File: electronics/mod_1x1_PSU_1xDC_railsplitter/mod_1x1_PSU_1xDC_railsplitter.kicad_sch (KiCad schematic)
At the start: 11 parts, among them J1 module_2x15_left_input, J2 module_2x15_right_input, J3 Jack-DC, J5 Conn_01x02

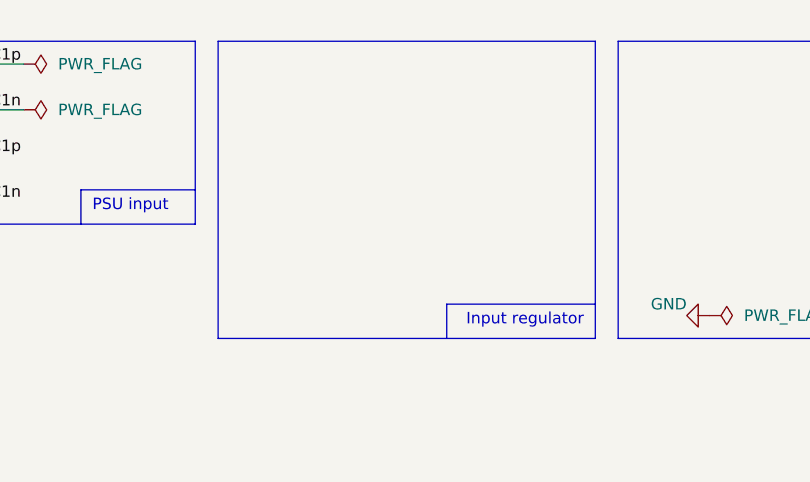
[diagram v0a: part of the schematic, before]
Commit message: WIP initial LDO schematic, updated PCB library
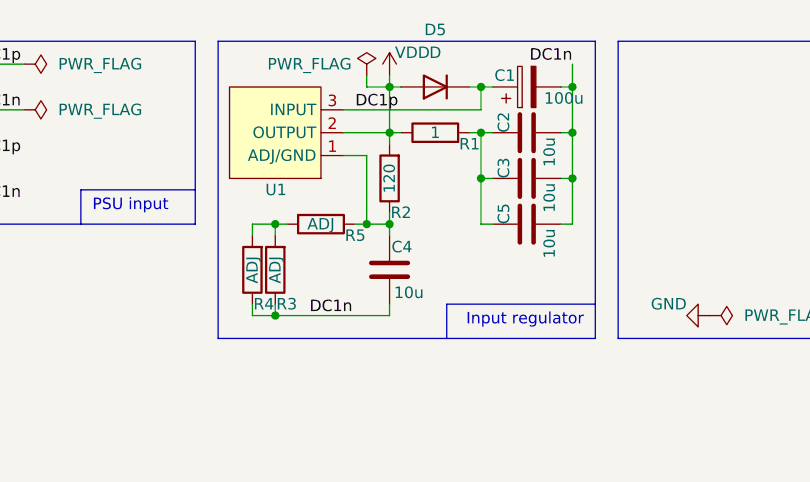
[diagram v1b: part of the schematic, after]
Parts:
- added C1: 100u, SquantorRcl:C-050-100-elco, symbol Device:C_Polarized
- added C2, C3, C4, C5: 10u, SquantorRcl:C_0805, symbol Device:C
- added D5: D, SquantorDiodes:SOD-323-onsemi, symbol Device:D
- added R1: 1, SquantorRcl:R_0805+0603, symbol Device:R
- added R2: 120, SquantorRcl:R_0805+0603, symbol Device:R
- added R3, R4, R5: ADJ, SquantorRcl:R_0805+0603, symbol Device:R
- added U1: ~, SquantorIC:TO-252_D-PAK_IRF, symbol SquantorGenericAnalog:LM1117
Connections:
- net DC1n: now also C1.2, C2.2, C3.2, C4.1, C5.2, R3.1, R4.1
- net DC1p: now also C1.1, D5.1 (K), U1.3 (INPUT)
- new net: C2.1, C3.1, C5.1, R1.2
- new net: C4.2, R2.1, R5.1, U1.1 (ADJ/GND)
- new net: R3.2, R4.2, R5.2
- new net VDD: D5.2 (A), R1.1, R2.2, U1.2 (OUTPUT)

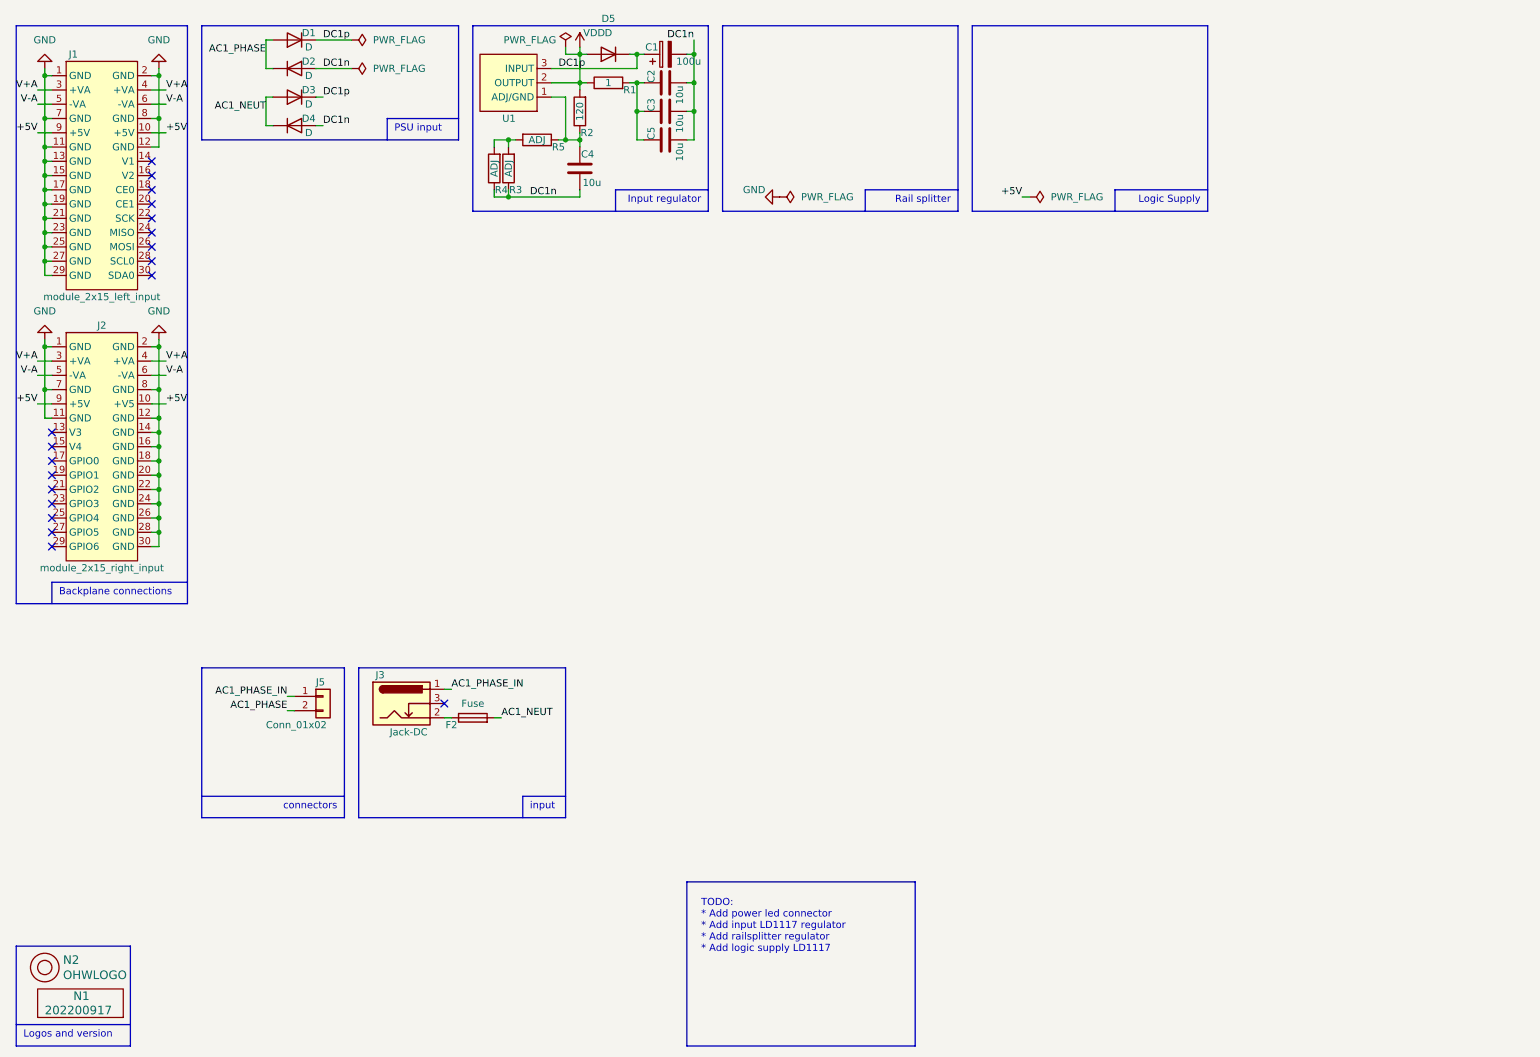
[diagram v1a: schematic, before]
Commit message: WIP schematic entry
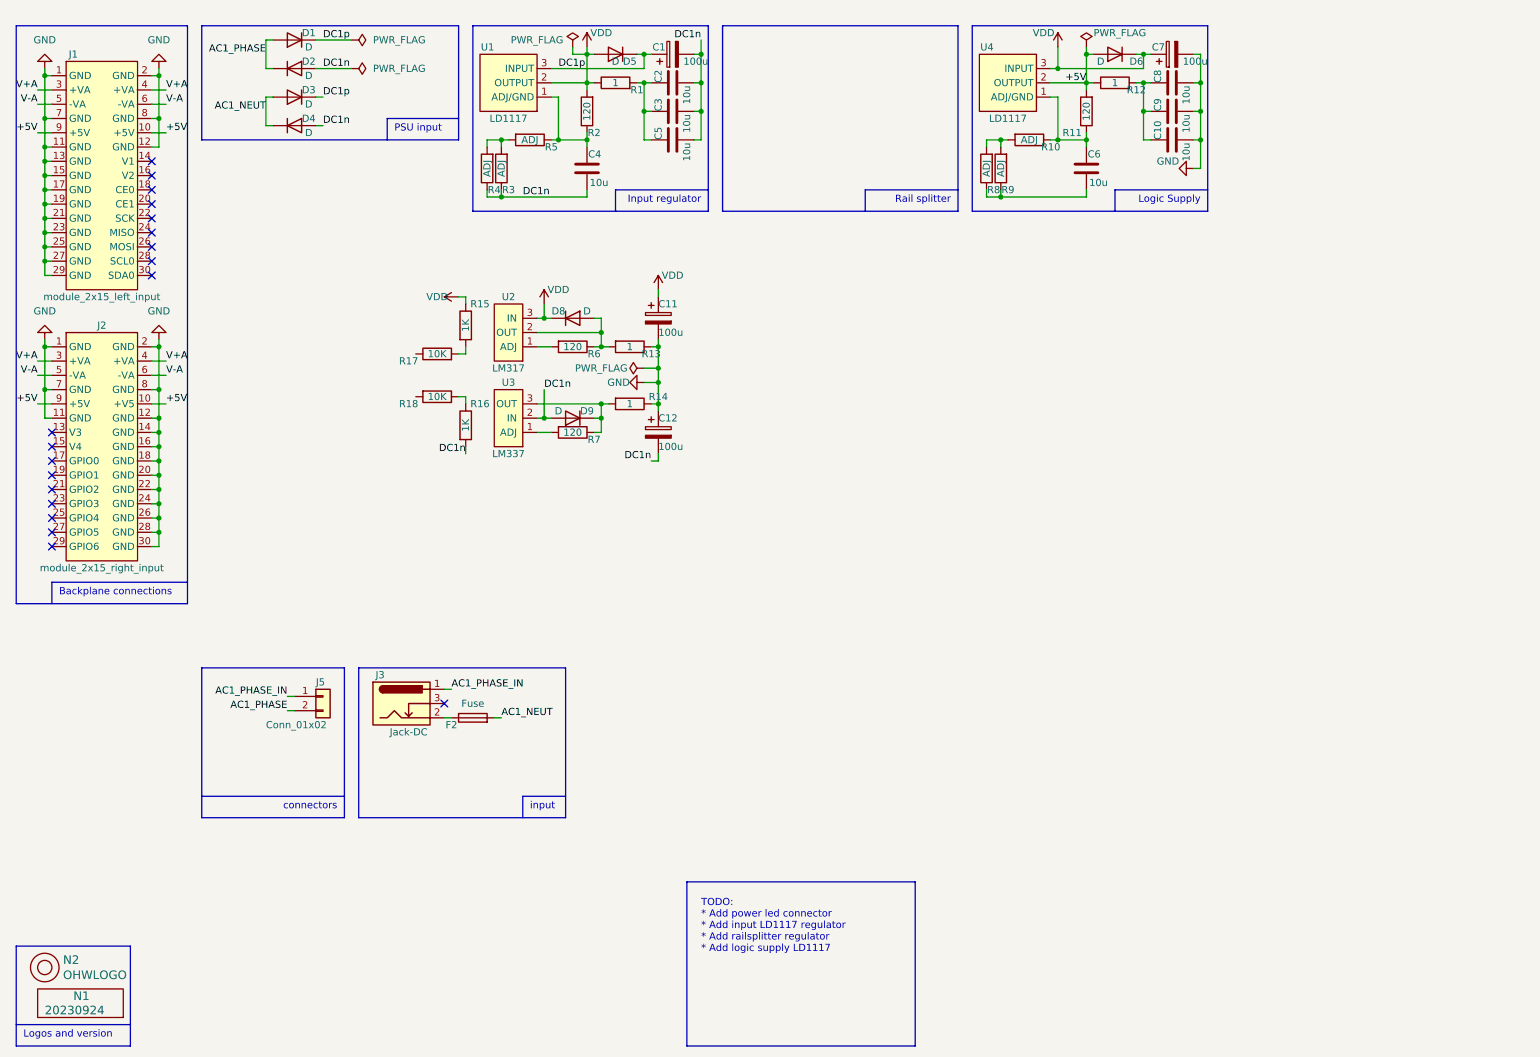
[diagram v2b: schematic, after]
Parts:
- added C10, C6, C8, C9: 10u, SquantorRcl:C_0805, symbol Device:C
- added C11, C12, C7: 100u, SquantorRcl:C-050-100-elco-lying, symbol Device:C_Polarized
- added D6, D8, D9: D, SquantorDiodes:SOD-323-onsemi, symbol Device:D
- added R10, R8, R9: ADJ, SquantorRcl:R_0805+0603, symbol Device:R
- added R11, R6, R7: 120, SquantorRcl:R_0805+0603, symbol Device:R
- added R12, R13, R14: 1, SquantorRcl:R_0805+0603, symbol Device:R
- added R15, R16: 1K, SquantorRcl:R_0805+0603, symbol Device:R
- added R17, R18: 10K, SquantorRcl:R_0805+0603, symbol Device:R
- added U2: LM317, SquantorIC:TO-252_D-PAK_IRF, symbol SquantorGenericAnalog:LM317
- added U3: LM337, SquantorIC:TO-252_D-PAK_IRF, symbol SquantorGenericAnalog:LM337
- added U4: LD1117, SquantorIC:TO-252_D-PAK_IRF, symbol SquantorGenericAnalog:LM1117
- C1: footprint SquantorRcl:C-050-100-elco -> SquantorRcl:C-050-100-elco-lying
- N1: value 202200917 -> 20230924
- U1: value ~ -> LD1117
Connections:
- net +5V: now also D6.2 (A), R11.2, R12.1, U4.2 (OUTPUT)
- net DC1n: now also C12.2, D9.2 (A), R16.2, U3.2 (IN)
- net GND: now also C10.2, C11.2, C12.1, C7.2, C8.2, C9.2, R13.1, R14.1
- net VDD: now also C11.1, C7.1, D6.1 (K), D8.1 (K), R15.1, U2.3 (IN), U4.3 (INPUT)
- new net: R7.2, U3.1 (ADJ)
- new net: D9.1 (K), R14.2, R7.1, U3.3 (OUT)
- new net: D8.2 (A), R13.2, R6.1, U2.2 (OUT)
- new net: R15.2, R17.2
- new net: C6.2, R10.1, R11.1, U4.1 (ADJ/GND)
- new net: R10.2, R8.2, R9.2
- new net: C6.1, R8.1, R9.1
- new net: C10.1, C8.1, C9.1, R12.2
- new net: R16.1, R18.1
- new net: R6.2, U2.1 (ADJ)
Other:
- moved on the sheet: C1, C2, C3, C4, C5, D5, R1, R2, R3, R4, R5

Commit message: small schematic updates and place and route
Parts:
- added RV1: 1K, Potentiometer_THT:Potentiometer_Bourns_3386P_Vertical, symbol Device:R_Potentiometer
- C1: footprint SquantorRcl:C-050-100-elco-lying -> SquantorRcl:C-050-100-elco-lying_flip
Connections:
- net GND: now also C6.1, R8.1, R9.1
- net at R17.1: now also R15.2
- net at R17.2: now also RV1.1; no longer R15.2
- net at R18.2: now also RV1.3
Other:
- moved on the sheet: R15, R16, R17, R18

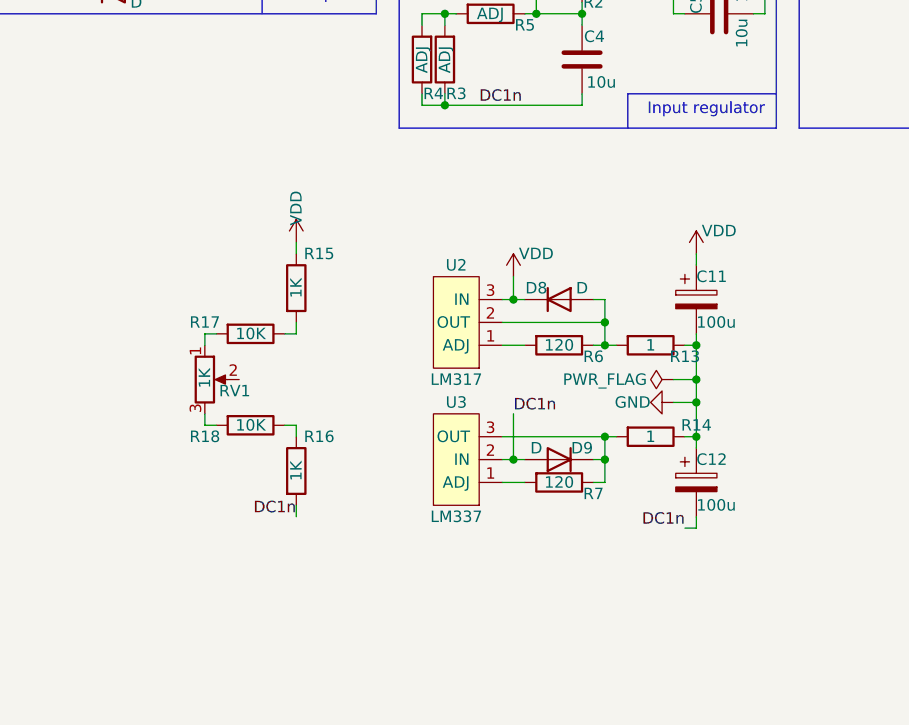
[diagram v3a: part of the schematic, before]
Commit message: WIP placement, done schematic
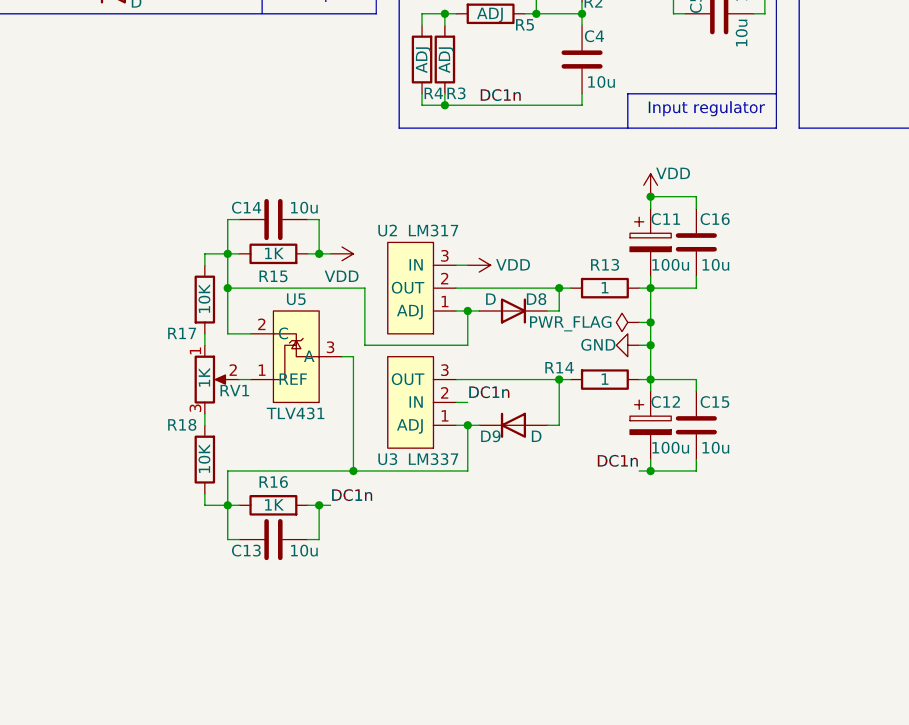
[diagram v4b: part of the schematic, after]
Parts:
- removed R6, R7: 120, SquantorRcl:R_0805+0603, symbol Device:R
- added C13, C14, C15, C16: 10u, SquantorRcl:C_0603, symbol Device:C
- added U5: TLV431, SquantorIC:SOT23-3, symbol SquantorGenericAnalog:TL431_SOT-23
- C11, C12: footprint SquantorRcl:C-050-100-elco-lying -> SquantorRcl:C-050-100-elco-lying_flip
- R15, R16, R17, R18: footprint SquantorRcl:R_0805+0603 -> SquantorRcl:R_0603_hand
- RV1: footprint Potentiometer_THT:Potentiometer_Bourns_3386P_Vertical -> SquantorRcl:POT-Bourns-3362P
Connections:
- net DC1n: now also C13.2, C15.1; no longer D9.2 (A)
- net GND: now also C15.2, C16.1
- net VDD: now also R15.2, C14.2, C16.2; no longer D8.1 (K), R15.1
- net at U3.1 (ADJ): now also D9.1 (K), R16.1, R18.1, C13.1, U5.3 (A)
- net at R14.2, U3.3 (OUT): now also D9.2 (A); no longer D9.1 (K)
- net at R13.2, U2.2 (OUT): now also D8.1 (K); no longer D8.2 (A)
- net at R17.1: now also D8.2 (A), R15.1, U2.1 (ADJ), C14.1, U5.2 (C); no longer R15.2
- net at RV1.2: now also U5.1 (REF)
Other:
- moved on the sheet: C11, C12, D8, D9, R13, R14, R15, R16, R17, R18, U2, U3

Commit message: further placing and routing
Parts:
- RV1: footprint SquantorRcl:POT-Bourns-3362P -> SquantorRcl:POT-23A-BI_technologies
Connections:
- net DC1n is gone; now on net V-A: C1.2, C12.2, C13.2, C15.1, C2.2, C3.2, C4.1, C5.2, D2.2 (A), D4.2 (A), R16.2, R3.1, R4.1, U3.2 (IN)
- net V+A: now also C11.1, C14.2, C16.2, C7.1, D5.2 (A), D6.1 (K), R1.1, R15.2, R2.2, U1.2 (OUTPUT), U4.3 (INPUT)
- net VDD: no longer C11.1, C14.2, C16.2, C7.1, D5.2 (A), D6.1 (K), R1.1, R15.2, R2.2, U1.2 (OUTPUT), U4.3 (INPUT)
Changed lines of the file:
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@@
   (junction (at 189.23 44.45) (diameter 0) (color 0 0 0 0)
-  )
-  (junction (at 123.19 54.61) (diameter 0) (color 0 0 0 0)
   )
   (junction (at 125.73 24.13) (diameter 0) (color 0 0 0 0)
@@
     (effects (font (size 1.27 1.27)) (justify right bottom))
   )
+  (label "V+A" (at 115.57 17.78 0) (fields_autoplaced)
+    (effects (font (size 1.27 1.27)) (justify left bottom))
+  )
   (label "+5V" (at 17.78 33.02 180) (fields_autoplaced)
     (effects (font (size 1.27 1.27)) (justify right bottom))
   )
-  (label "DC1n" (at 102.87 77.47 0) (fields_autoplaced)
+  (label "V-A" (at 121.92 85.09 180) (fields_autoplaced)
+    (effects (font (size 1.27 1.27)) (justify right bottom))
+  )
+  (label "V+A" (at 199.39 17.78 0) (fields_autoplaced)
     (effects (font (size 1.27 1.27)) (justify left bottom))
   )
@@
     (effects (font (size 1.27 1.27)) (justify left bottom))
   )
+  (label "V-A" (at 87.63 88.9 0) (fields_autoplaced)
+    (effects (font (size 1.27 1.27)) (justify left bottom))
+  )
   (label "AC1_NEUT" (at 58.42 29.21 180) (fields_autoplaced)
     (effects (font (size 1.27 1.27)) (justify right bottom))
@@
     (effects (font (size 1.27 1.27)) (justify right bottom))
   )
-  (label "DC1n" (at 68.58 31.75 0) (fields_autoplaced)
+  (label "V+A" (at 87.63 60.96 0) (fields_autoplaced)
     (effects (font (size 1.27 1.27)) (justify left bottom))
   )
@@
     (effects (font (size 1.27 1.27)) (justify left bottom))
   )
-  (label "DC1n" (at 135.89 16.51 180) (fields_autoplaced)
+  (label "V-A" (at 135.89 16.51 180) (fields_autoplaced)
     (effects (font (size 1.27 1.27)) (justify right bottom))
   )
@@
     (effects (font (size 1.27 1.27)) (justify left bottom))
   )
-  (label "DC1n" (at 68.58 21.59 0) (fields_autoplaced)
+  (label "V-A" (at 105.41 44.45 0) (fields_autoplaced)
     (effects (font (size 1.27 1.27)) (justify left bottom))
   )
@@
     (effects (font (size 1.27 1.27)) (justify right bottom))
   )
-  (label "DC1n" (at 121.92 85.09 180) (fields_autoplaced)
-    (effects (font (size 1.27 1.27)) (justify right bottom))
-  )
-  (label "DC1n" (at 104.14 44.45 0) (fields_autoplaced)
+  (label "V-A" (at 68.58 31.75 0) (fields_autoplaced)
     (effects (font (size 1.27 1.27)) (justify left bottom))
   )
@@
     (effects (font (size 1.27 1.27)) (justify right bottom))
   )
+  (label "V+A" (at 124.46 54.61 0) (fields_autoplaced)
+    (effects (font (size 1.27 1.27)) (justify left bottom))
+  )
   (label "V+A" (at 17.78 73.66 180) (fields_autoplaced)
     (effects (font (size 1.27 1.27)) (justify right bottom))
@@
     (effects (font (size 1.27 1.27)) (justify left bottom))
   )
+  (label "V-A" (at 102.87 77.47 0) (fields_autoplaced)
+    (effects (font (size 1.27 1.27)) (justify left bottom))
+  )
   (label "V+A" (at 17.78 25.4 180) (fields_autoplaced)
     (effects (font (size 1.27 1.27)) (justify right bottom))
@@
     (effects (font (size 1.27 1.27)) (justify left bottom))
   )
-  (label "DC1n" (at 87.63 88.9 0) (fields_autoplaced)
+  (label "V-A" (at 68.58 21.59 0) (fields_autoplaced)
     (effects (font (size 1.27 1.27)) (justify left bottom))
   )
@@
         (path "/646d9e91-59b4-4865-a2fc-29780ed32563"
           (reference "D1") (unit 1)
-        )
-      )
-    )
-  )
-  (symbol (lib_id "power:VDD") (at 199.39 17.78 0) (unit 1)
-    (in_bom yes) (on_board yes) (dnp no)
-    (property "Reference" "#PWR02" (at 199.39 21.59 0)
-      (effects (font (size 1.27 1.27)) hide)
-    )
-    (property "Value" "VDD" (at 196.85 15.24 0)
-      (effects (font (size 1.27 1.27)))
-    )
-    (property "Footprint" "" (at 199.39 17.78 0)
-      (effects (font (size 1.27 1.27)) hide)
-    )
-    (property "Datasheet" "" (at 199.39 17.78 0)
-      (effects (font (size 1.27 1.27)) hide)
-    )
-    (pin "1")
-    (instances
-      (project "mod_1x1_PSU_1xDC_railsplitter"
-        (path "/646d9e91-59b4-4865-a2fc-29780ed32563"
-          (reference "#PWR02") (unit 1)
         )
       )
@@
     )
   )
-  (symbol (lib_id "power:VDD") (at 123.19 54.61 0) (unit 1)
-    (in_bom yes) (on_board yes) (dnp no)
-    (property "Reference" "#PWR06" (at 123.19 58.42 0)
-      (effects (font (size 1.27 1.27)) hide)
-    )
-    (property "Value" "VDD" (at 125.73 52.07 0)
-      (effects (font (size 1.27 1.27)))
-    )
-    (property "Footprint" "" (at 123.19 54.61 0)
-      (effects (font (size 1.27 1.27)) hide)
-    )
-    (property "Datasheet" "" (at 123.19 54.61 0)
-      (effects (font (size 1.27 1.27)) hide)
-    )
-    (pin "1")
-    (instances
-      (project "mod_1x1_PSU_1xDC_railsplitter"
-        (path "/646d9e91-59b4-4865-a2fc-29780ed32563"
-          (reference "#PWR06") (unit 1)
-        )
-      )
-    )
-  )
   (symbol (lib_id "power:PWR_FLAG") (at 121.92 68.58 90) (unit 1)
     (in_bom yes) (on_board yes) (dnp no)
@@
       (effects (font (size 1.27 1.27)) (justify right))
     )
-    (property "Footprint" "SquantorRcl:POT-Bourns-3362P" (at 73.66 74.93 0)
+    (property "Footprint" "SquantorRcl:POT-23A-BI_technologies" (at 73.66 74.93 0)
       (effects (font (size 1.27 1.27)) hide)
     )
@@
     )
   )
-  (symbol (lib_id "power:VDD") (at 115.57 17.78 0) (unit 1)
-    (in_bom yes) (on_board yes) (dnp no)
-    (property "Reference" "#PWR01" (at 115.57 21.59 0)
-      (effects (font (size 1.27 1.27)) hide)
-    )
-    (property "Value" "VDD" (at 118.11 15.24 0)
-      (effects (font (size 1.27 1.27)))
-    )
-    (property "Footprint" "" (at 115.57 17.78 0)
-      (effects (font (size 1.27 1.27)) hide)
-    )
-    (property "Datasheet" "" (at 115.57 17.78 0)
-      (effects (font (size 1.27 1.27)) hide)
-    )
-    (pin "1")
-    (instances
-      (project "mod_1x1_PSU_1xDC_railsplitter"
-        (path "/646d9e91-59b4-4865-a2fc-29780ed32563"
-          (reference "#PWR01") (unit 1)
-        )
-      )
-    )
-  )
   (symbol (lib_id "Device:C") (at 130.81 24.13 90) (unit 1)
     (in_bom yes) (on_board yes) (dnp no)
@@
         )
       )
-    )
-  )
-  (symbol (lib_id "power:VDD") (at 87.63 60.96 270) (unit 1)
-    (in_bom yes) (on_board yes) (dnp no)
-    (property "Reference" "#PWR07" (at 83.82 60.96 0)
-      (effects (font (size 1.27 1.27)) hide)
-    )
-    (property "Value" "VDD" (at 88.9 63.5 90)
-      (effects (font (size 1.27 1.27)))
-    )
-    (property "Footprint" "" (at 87.63 60.96 0)
-      (effects (font (size 1.27 1.27)) hide)
-    )
-    (property "Datasheet" "" (at 87.63 60.96 0)
-      (effects (font (size 1.27 1.27)) hide)
-    )
-    (pin "1")
-    (instances
-      (project "mod_1x1_PSU_1xDC_railsplitter"
-        (path "/646d9e91-59b4-4865-a2fc-29780ed32563"
-          (reference "#PWR07") (unit 1)
-        )
-      )

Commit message: completed silk placement, few values adjusted
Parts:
- N1: value 20230924 -> 20231003
- R1, R12: value 1 -> 2.2
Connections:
- net VDD is gone; now on net V+A: U2.3 (IN)
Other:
- moved on the sheet: C10, C11, C12, C13, C14, C15, C16, C6, C7, C8, C9, D6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
